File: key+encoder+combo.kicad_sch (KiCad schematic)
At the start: 2 parts, among them SW13 SW_Push

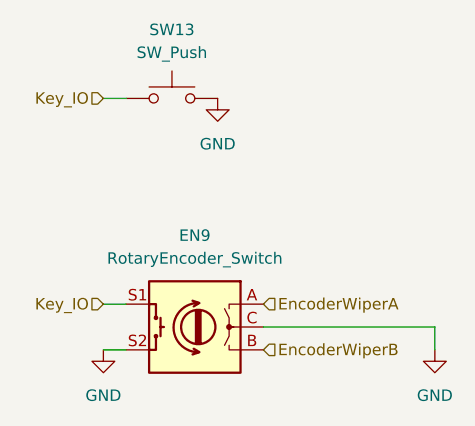
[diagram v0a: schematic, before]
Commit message: initial board routing
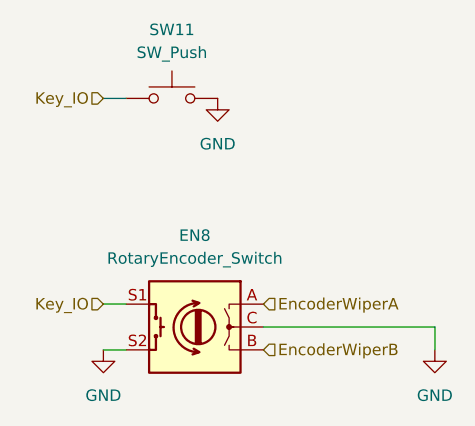
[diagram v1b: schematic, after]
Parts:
- renumbered EN9 to EN8, SW13 to SW11
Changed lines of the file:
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@@
   (symbol (lib_id "power:GND") (at 146.05 96.52 0)
     (in_bom yes) (on_board yes) (fields_autoplaced)
-    (property "Reference" "#PWR0117" (id 0) (at 146.05 102.87 0)
+    (property "Reference" "#PWR026" (id 0) (at 146.05 102.87 0)
       (effects (font (size 1.27 1.27)) hide)
     )
@@
   (symbol (lib_id "power:GND") (at 170.18 124.46 0)
     (in_bom yes) (on_board yes) (fields_autoplaced)
-    (property "Reference" "#PWR0108" (id 0) (at 170.18 130.81 0)
+    (property "Reference" "#PWR027" (id 0) (at 170.18 130.81 0)
       (effects (font (size 1.27 1.27)) hide)
     )
@@
   (symbol (lib_id "Device:RotaryEncoder_Switch") (at 143.51 121.92 0) (mirror y)
     (in_bom yes) (on_board yes) (fields_autoplaced)
-    (property "Reference" "EN9" (id 0) (at 143.51 111.76 0))
+    (property "Reference" "EN8" (id 0) (at 143.51 111.76 0))
     (property "Value" "RotaryEncoder_Switch" (id 1) (at 143.51 114.3 0))
     (property "Footprint" "Keeby-Cat Footprints:RotaryEncoder_Alps_EC11E-Switch_Vertical_H20mm_nomount_alt" (id 2) (at 147.32 117.856 0)
@@
   (symbol (lib_id "power:GND") (at 133.35 124.46 0)
     (in_bom yes) (on_board yes) (fields_autoplaced)
-    (property "Reference" "#PWR0116" (id 0) (at 133.35 130.81 0)
+    (property "Reference" "#PWR025" (id 0) (at 133.35 130.81 0)
       (effects (font (size 1.27 1.27)) hide)
     )
@@
   (symbol (lib_id "Switch:SW_Push") (at 140.97 96.52 0)
     (in_bom yes) (on_board yes) (fields_autoplaced)
-    (property "Reference" "SW13" (id 0) (at 140.97 88.9 0))
+    (property "Reference" "SW11" (id 0) (at 140.97 88.9 0))
     (property "Value" "SW_Push" (id 1) (at 140.97 91.44 0))
     (property "Footprint" "Keeby-Cat Footprints:CherryMX_1u_north_potcombo" (id 2) (at 140.97 91.44 0)

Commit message: shrank board outline to 100mm max
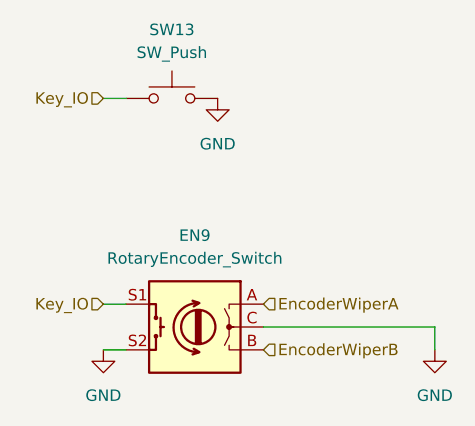
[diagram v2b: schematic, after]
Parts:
- renumbered EN8 to EN9, SW11 to SW13
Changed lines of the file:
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@@
   (symbol (lib_id "power:GND") (at 146.05 96.52 0)
     (in_bom yes) (on_board yes) (fields_autoplaced)
-    (property "Reference" "#PWR026" (id 0) (at 146.05 102.87 0)
+    (property "Reference" "#PWR0117" (id 0) (at 146.05 102.87 0)
       (effects (font (size 1.27 1.27)) hide)
     )
@@
   (symbol (lib_id "power:GND") (at 170.18 124.46 0)
     (in_bom yes) (on_board yes) (fields_autoplaced)
-    (property "Reference" "#PWR027" (id 0) (at 170.18 130.81 0)
+    (property "Reference" "#PWR0108" (id 0) (at 170.18 130.81 0)
       (effects (font (size 1.27 1.27)) hide)
     )
@@
   (symbol (lib_id "Device:RotaryEncoder_Switch") (at 143.51 121.92 0) (mirror y)
     (in_bom yes) (on_board yes) (fields_autoplaced)
-    (property "Reference" "EN8" (id 0) (at 143.51 111.76 0))
+    (property "Reference" "EN9" (id 0) (at 143.51 111.76 0))
     (property "Value" "RotaryEncoder_Switch" (id 1) (at 143.51 114.3 0))
     (property "Footprint" "Keeby-Cat Footprints:RotaryEncoder_Alps_EC11E-Switch_Vertical_H20mm_nomount_alt" (id 2) (at 147.32 117.856 0)
@@
   (symbol (lib_id "power:GND") (at 133.35 124.46 0)
     (in_bom yes) (on_board yes) (fields_autoplaced)
-    (property "Reference" "#PWR025" (id 0) (at 133.35 130.81 0)
+    (property "Reference" "#PWR0116" (id 0) (at 133.35 130.81 0)
       (effects (font (size 1.27 1.27)) hide)
     )
@@
   (symbol (lib_id "Switch:SW_Push") (at 140.97 96.52 0)
     (in_bom yes) (on_board yes) (fields_autoplaced)
-    (property "Reference" "SW11" (id 0) (at 140.97 88.9 0))
+    (property "Reference" "SW13" (id 0) (at 140.97 88.9 0))
     (property "Value" "SW_Push" (id 1) (at 140.97 91.44 0))
     (property "Footprint" "Keeby-Cat Footprints:CherryMX_1u_north_potcombo" (id 2) (at 140.97 91.44 0)

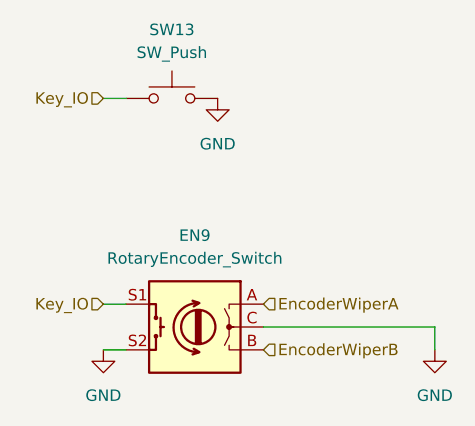
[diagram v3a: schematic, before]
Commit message: adjust schematic graphics
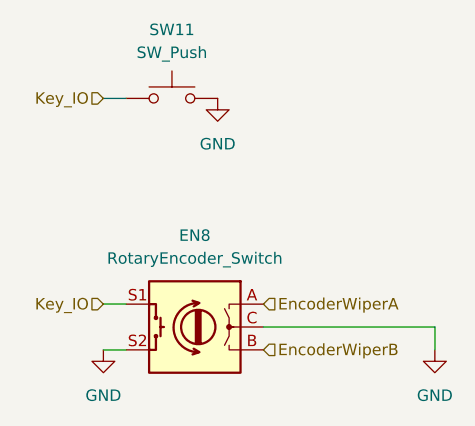
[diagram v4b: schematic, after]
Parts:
- renumbered EN9 to EN8, SW13 to SW11
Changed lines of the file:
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@@
     (effects (font (size 1.27 1.27)) (justify left))
   )
-  (symbol (lib_id "Switch:SW_Push") (at 140.97 96.52 0)
+  (symbol (lib_id "Switch:SW_Push") (at 140.97 96.52 0) (unit 1)
     (in_bom yes) (on_board yes) (fields_autoplaced)
-    (property "Reference" "SW13" (id 0) (at 140.97 88.9 0))
+    (property "Reference" "SW11" (id 0) (at 140.97 88.9 0))
     (property "Value" "SW_Push" (id 1) (at 140.97 91.44 0))
     (property "Footprint" "Keeby-Cat Footprints:CherryMX_1u_north_potcombo" (id 2) (at 140.97 91.44 0)
@@
     (pin "2")
   )
-  (symbol (lib_id "power:GND") (at 170.18 124.46 0)
+  (symbol (lib_id "power:GND") (at 170.18 124.46 0) (unit 1)
     (in_bom yes) (on_board yes) (fields_autoplaced)
-    (property "Reference" "#PWR0108" (id 0) (at 170.18 130.81 0)
+    (property "Reference" "#PWR027" (id 0) (at 170.18 130.81 0)
       (effects (font (size 1.27 1.27)) hide)
     )
@@
     (pin "1")
   )
-  (symbol (lib_id "Device:RotaryEncoder_Switch") (at 143.51 121.92 0) (mirror y)
+  (symbol (lib_id "Device:RotaryEncoder_Switch") (at 143.51 121.92 0) (mirror y) (unit 1)
     (in_bom yes) (on_board yes) (fields_autoplaced)
-    (property "Reference" "EN9" (id 0) (at 143.51 111.76 0))
+    (property "Reference" "EN8" (id 0) (at 143.51 111.76 0))
     (property "Value" "RotaryEncoder_Switch" (id 1) (at 143.51 114.3 0))
     (property "Footprint" "Keeby-Cat Footprints:RotaryEncoder_Alps_EC11E-Switch_Vertical_H20mm_nomount_alt" (id 2) (at 147.32 117.856 0)
@@
     (pin "S2")
   )
-  (symbol (lib_id "power:GND") (at 133.35 124.46 0)
+  (symbol (lib_id "power:GND") (at 133.35 124.46 0) (unit 1)
     (in_bom yes) (on_board yes) (fields_autoplaced)
-    (property "Reference" "#PWR0116" (id 0) (at 133.35 130.81 0)
+    (property "Reference" "#PWR025" (id 0) (at 133.35 130.81 0)
       (effects (font (size 1.27 1.27)) hide)
     )
@@
     (pin "1")
   )
-  (symbol (lib_id "power:GND") (at 146.05 96.52 0)
+  (symbol (lib_id "power:GND") (at 146.05 96.52 0) (unit 1)
     (in_bom yes) (on_board yes) (fields_autoplaced)
-    (property "Reference" "#PWR0117" (id 0) (at 146.05 102.87 0)
+    (property "Reference" "#PWR026" (id 0) (at 146.05 102.87 0)
       (effects (font (size 1.27 1.27)) hide)
     )
